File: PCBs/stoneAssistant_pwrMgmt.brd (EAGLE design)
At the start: 66 x 55.9 mm, 56 parts, among them IC1 TINY2313-*S*, IC2 CNY17, IC3 CPC1976Y, IC4 CPC1976Y, T4 IRLML6402, X1 N, X2 L, X3 BTN_ON, X4 12V, X5 GND

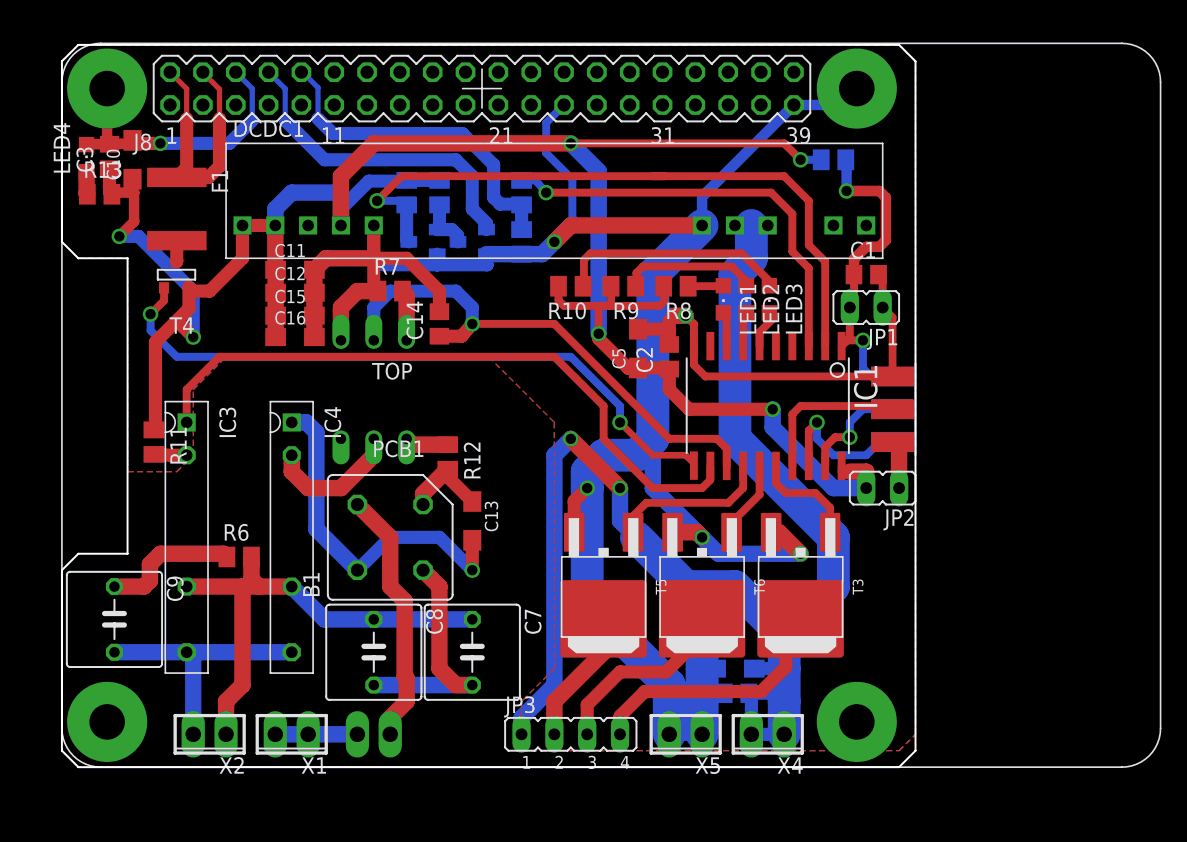
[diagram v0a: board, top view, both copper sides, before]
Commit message: electrical: pcb redesign for better fit of components, transistor level shifter moved away from dc/dc, smd rectifier instead of tht one, cancelled out snubber, isp moved away from edge so the attiny can be programmed with the board installed on the raspberry pi
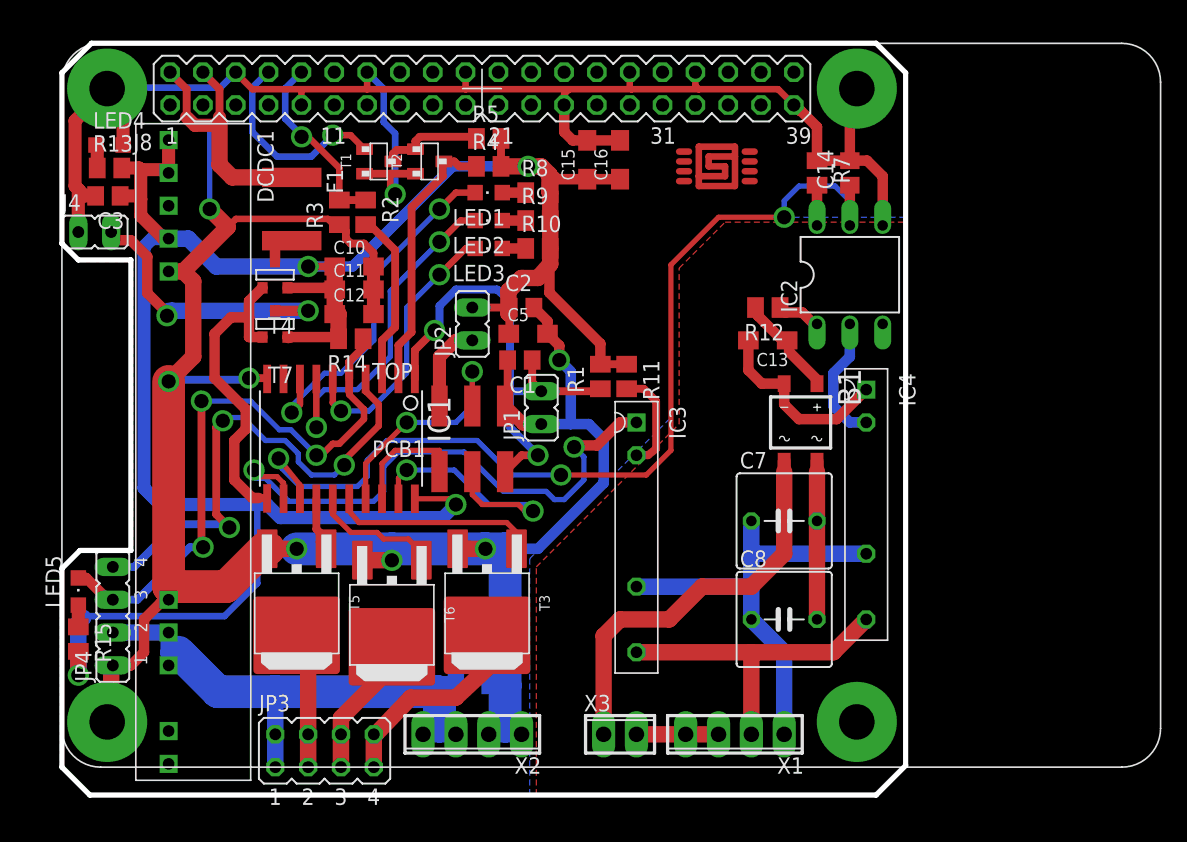
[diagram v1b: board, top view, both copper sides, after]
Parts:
- removed C9: 82n, rcl:C050-075X075
- removed R6: 33R, rcl:M0805
- removed X4: 12V, con-phoenix-254:2POL254
- removed X5: GND, con-phoenix-254:2POL254
- added J4: DISPLAY, jumper:JP1
- added JP4: FAN, jumper:JP4
- added LED5: (no value), led:CHIPLED_0805
- added R14: 18k, rcl:M0805
- added R15: 270R, rcl:M0805
- added T7: IRLML6402, IRLML6402:SOT-23
- B1: value (none) -> B4S; device rectifier:1KAB -> rectifier:MBS
- JP3: device jumper:JP4 -> jumper:JP4Q
- R4, R5: value 18k -> 1k
- U$2: value AVR-ISP-6-EDGE -> AVR_ISPSINGLESIDED_SMD; device avr-7:6PAD_ISP -> stoneTronics:PINHEADER_254_2X3_SMD
- X1: value N -> (none); device con-phoenix-254:2POL254 -> con-phoenix-254:4POL254
- X2: value L -> (none); device con-phoenix-254:2POL254 -> con-phoenix-254:4POL254
- moved IC4 44.5 mm to (62.2, 20.3)
- moved IC2 37.9 mm to (61.0, 38.1), flipped to the top
- moved R11 36.9 mm to (43.7, 30.2)
- moved DCDC1 36.0 mm to (9.53, 23.1), turned to 270 degrees
- moved IC3 34.8 mm to (44.5, 17.8)
- moved X1 34.3 mm to (52.1, 2.54)
- moved R7 34.3 mm to (58.4, 46.0), turned to 270 degrees
- moved JP2 34.2 mm to (31.8, 34.3), turned to 0 degrees
- moved C14 33.8 mm to (61.0, 46.0)
- moved IC1 33.1 mm to (21.6, 25.4)
- moved B1 33.0 mm to (57.1, 26.7), turned to 180 degrees
- moved C8 31.9 mm to (55.9, 11.4), turned to 0 degrees
- moved U$2 31.4 mm to (33.0, 24.1), flipped to the top, turned to 0 degrees
- moved C16 28.6 mm to (43.2, 47.0), turned to 90 degrees
- moved C1 27.6 mm to (35.4, 31.5), turned to 180 degrees
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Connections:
- removed net N$32: C9.1, R6.1
- new net FAN_PWM: IC1.4, JP4.4
- new net FAN_SIGNAL: IC1.5, JP4.3, LED5.C, R14.1
- new net N$24: J4.2, T7.3
- new net N$25: LED5.A, R15.1
- net +12V: now also JP3.2, JP4.2, X2.3, X2.4; no longer X4.1, X4.2
- net +5V: now also R14.2, R15.2, T7.2
- net GND: now also J4.1, JP4.1, PCB1.PE_BL, U$2.P$6, X2.1, X2.2; no longer U$2.GND, X5.1, X5.2
- net N$1: now also U$2.P$3; no longer U$2.RST
- net N$10: now also X1.2; no longer C9.2, X2.2
- net N$11: now also X1.1; no longer R6.2, X2.1
- net N$12: now also X1.3, X1.4; no longer X1.1, X1.2
- net N$21: now also JP3.3, JP3.4; no longer JP3.2
- net N$22: now also JP3.5, JP3.6; no longer JP3.3
- net N$23: now also JP3.7, JP3.8; no longer JP3.4
- net N$6: now also U$2.P$2; no longer U$2.SCK
- net N$7: now also U$2.P$1; no longer U$2.MISO
- net N$8: now also U$2.P$7; no longer U$2.MOSI
- net N$9: now also U$2.P$8; no longer U$2.VCC
- net RPI_SUPPLY: now also T7.1
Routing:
- net +12V: track 108.3 -> 45.3 mm, vias 2 -> 0
- net GND: track 236.8 -> 297.1 mm, vias 6 -> 8
- net FAN_SIGNAL: track 0.00 -> 46.0 mm, vias 0 -> 3
- net FAN_PWM: track 0.00 -> 39.8 mm, vias 0 -> 3
- net BUTTON: track 40.5 -> 76.3 mm, vias 1 -> 3
- net N$3: track 53.0 -> 21.1 mm, vias 1 -> 0
- net RPI_SUPPLY: track 50.9 -> 24.3 mm, vias 2 -> 0
- net LED_SHDWN: track 2.67 -> 27.4 mm, vias 0 -> 2
- net LED_RUN: track 2.73 -> 27.0 mm, vias 0 -> 2
- net N$24: track 0.00 -> 22.7 mm, vias 0 -> 2
- net N$2: track 32.8 -> 13.5 mm, vias 1 -> 0
- net N$26: track 0.00 -> 18.5 mm
- net LED_UART: track 3.09 -> 21.3 mm, vias 0 -> 2
- net N$36: track 18.2 -> 1.81 mm
- net N$1: track 25.1 -> 38.4 mm
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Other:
- board size 66 x 55.9 mm -> 65.3 x 58.2 mm
- board text added: "pwr&pwm"
- board text added: "stoneAssistant"
- board text added: "stonetronics"

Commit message: final power management pcb
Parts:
- removed JP4: FAN, jumper:JP4
- removed LED5: (no value), led:CHIPLED_0805
- removed R14: 18k, rcl:M0805
- removed R15: 270R, rcl:M0805
- added T8: IRLML6402, IRLML6402:SOT-23
- added T9: IRLML2502, nxs_transistor:SOT-23
- added X4: FAN, nxs_con-misc:2_2.54MM
- added X5: GND, nxs_con-misc:2_2.54MM
- added X6: L, nxs_con-misc:2_2.54MM
- T3, T5, T6: value (none) -> IRLML2502; device we-transistor:DPAK_TO252 -> nxs_transistor:SOT-23
- X1: value (none) -> BTN_ON; device con-phoenix-254:4POL254 -> nxs_con-misc:2_2.54MM
- X2: value (none) -> +12V; device con-phoenix-254:4POL254 -> nxs_con-misc:2_2.54MM
- X3: value BTN_ON -> N; device con-phoenix-254:2POL254 -> nxs_con-misc:2_2.54MM
- moved LED4 45.2 mm to (31.6, 12.6)
- moved R13 42.3 mm to (31.6, 14.6)
- moved C3 42.0 mm to (45.5, 47.0), turned to 90 degrees
- moved X3 10.2 mm to (53.3, 2.03), turned to 180 degrees
- moved X1 8.90 mm to (43.2, 2.03)
- moved T3 8.57 mm to (26.3, 7.24), turned to 180 degrees
- moved T6 5.49 mm to (22.5, 7.24), turned to 180 degrees
- moved T5 5.48 mm to (18.7, 7.24), turned to 180 degrees
- moved X2 2.59 mm to (29.2, 2.03)
- moved JP3 0.89 mm to (21.2, 1.27)
- moved J4 0.89 mm to (2.54, 42.3)
- flipped C4 to the top, turned to 0 degrees
- flipped C6 to the top, turned to 0 degrees
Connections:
- removed net FAN_SIGNAL: IC1.5, JP4.3, LED5.C, R14.1
- new net 5V_FB: DCDC1.3, T8.3
- new net N$32: PCB1.2, T8.2
- net +12V: now also X2.1, X2.2, X4.1; no longer JP4.2, X2.3, X2.4
- net +5V: no longer R14.2, R15.2
- net FAN_PWM: now also T9.1; no longer JP4.4
- net GND: now also T3.2, T5.2, T6.2, T9.2, X5.1, X5.2; no longer JP4.1, T3.3, T5.3, T6.3, X2.1, X2.2
- net N$10: now also X6.2; no longer X1.2
- net N$11: now also X6.1; no longer X1.1
- net N$12: now also X1.2, X3.1; no longer X1.3, X1.4
- net N$16: now also X1.1; no longer X3.1
- net N$21: now also T5.3; no longer T5.2
- net N$22: now also T6.3; no longer T6.2
- net N$23: now also T3.3; no longer T3.2
- net N$25: now also T9.3, X4.2; no longer LED5.A, R15.1
- net RPI_5V: no longer PCB1.2
- net RPI_SUPPLY: now also T8.1
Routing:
- net FAN_SIGNAL: track 46.0 -> 0.00 mm, vias 3 -> 0
- net +5V: track 179.9 -> 158.7 mm, vias 4 -> 3
- net GND: track 297.1 -> 318.0 mm
- net RPI_SUPPLY: track 24.3 -> 42.9 mm, vias 0 -> 2
- net N$25: track 1.68 -> 18.8 mm, vias 0 -> 1
- net N$12: track 6.35 -> 20.4 mm
- net N$23: track 17.2 -> 6.81 mm
- net N$32: track 0.00 -> 10.2 mm
- net PWM_G: track 4.18 -> 14.0 mm
- net RPI_5V: track 20.5 -> 12.2 mm
- net +12V: track 45.3 -> 53.5 mm
- net 5V_FB: track 0.00 -> 8.01 mm
- net N$22: track 12.2 -> 6.14 mm
- net N$21: track 11.1 -> 6.67 mm
- net PWM_R: track 9.90 -> 13.5 mm
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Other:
- board size 65.3 x 58.2 mm -> 66.8 x 59.3 mm
- board text added: "+"
- board text added: "-"
- board text added: "14.6.2018"
- board text added: "B1"
- board text added: "C1"
- board text added: "C10"
- board text added: "C11"
- board text added: "C12"
- board text added: "C13"
- board text added: "C14"
- board text added: "C15"
- board text added: "C16"
- board text added: "C2"
- board text added: "C3"
- board text added: "C4"
- board text added: "C5"
- board text added: "C6"
- board text added: "C7"
- board text added: "C8"
- board text added: "DCDC1"
- board text added: "F1"
- board text added: "IC1"
- board text added: "IC2"
- board text added: "IC3"
- board text added: "IC4"
- board text added: "ICSP"
- board text added: "JP3"
- board text added: "LCD"
- board text added: "LED1"
- board text added: "LED2"
- board text added: "LED3"
- board text added: "LED4"
- board text added: "MAINS"
- board text added: "R1"
- board text added: "R10"
- board text added: "R11"
- board text added: "R12"
- board text added: "R13"
- board text added: "R2"
- board text added: "R3"
- board text added: "R4"
- board text added: "R5"
- board text added: "R7"
- board text added: "R8"
- board text added: "R9"
- board text added: "RST"
- board text added: "SUPPLY"
- board text added: "T1"
- board text added: "T2"
- board text added: "T3"
- board text added: "T4"
- board text added: "T5"
- board text added: "T6"
- board text added: "T7"
- board text added: "T8"
- board text added: "T9"
- board text added: "TARGET"
- board text added: "VOLTAGE"
- board text added: "X1"
- board text added: "X2"
- board text added: "X3"
- board text added: "X4"
- board text added: "X5"
- board text added: "X6"
- board text added: "by everyone"
- board text added: "free to use"
- board text added: "github.com/stonetronics"
- board text added: "pwr & pwm"
- board text removed: "pwr&pwm"

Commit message: move mechanical to thingiverse
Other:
- board text added: "for free use"
- board text removed: "free to use"
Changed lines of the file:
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@@
 <text x="35.433" y="48.514" size="1.016" layer="255" font="vector" ratio="15">R5</text>
 <text x="12.065" y="33.655" size="1.27" layer="255" font="vector" ratio="15">T7</text>
-<text x="12.065" y="37.465" size="1.27" layer="255" font="vector" ratio="15">T4</text>
+<text x="12.065" y="38.735" size="1.27" layer="255" font="vector" ratio="15">T4</text>
 <text x="33.782" y="13.97" size="1.27" layer="255" font="vector" ratio="15">R13</text>
 <text x="33.782" y="11.938" size="1.27" layer="255" font="vector" ratio="15">LED4</text>
@@
 <text x="0.762" y="39.624" size="1.27" layer="255" font="vector" ratio="15">-</text>
 <text x="3.302" y="39.497" size="1.27" layer="255" font="vector" ratio="15">+</text>
-<text x="45.72" y="40.64" size="1.27" layer="253" font="vector" ratio="15" rot="SMR0">free to use</text>
+<text x="45.72" y="40.64" size="1.27" layer="253" font="vector" ratio="15" rot="SMR0">for free use</text>
 <text x="45.72" y="38.735" size="1.27" layer="253" font="vector" ratio="15" rot="MR0">by everyone</text>
 </plain>
